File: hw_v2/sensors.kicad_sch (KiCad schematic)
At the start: 47 parts, among them U10 BMP280, U21 ADXL343, U23 MCP6004, U24 MCP6004, U6 TJA1051T-3

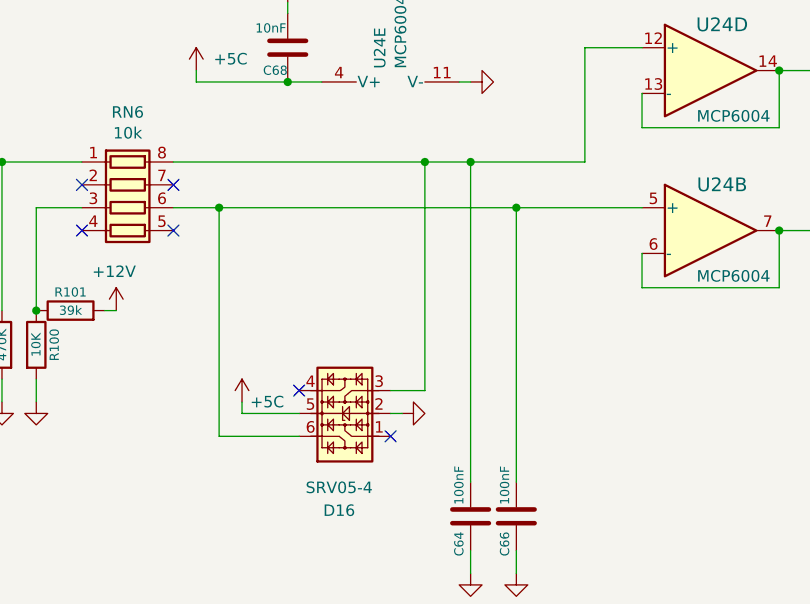
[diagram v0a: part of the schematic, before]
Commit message: wip routing iny/ign drivers
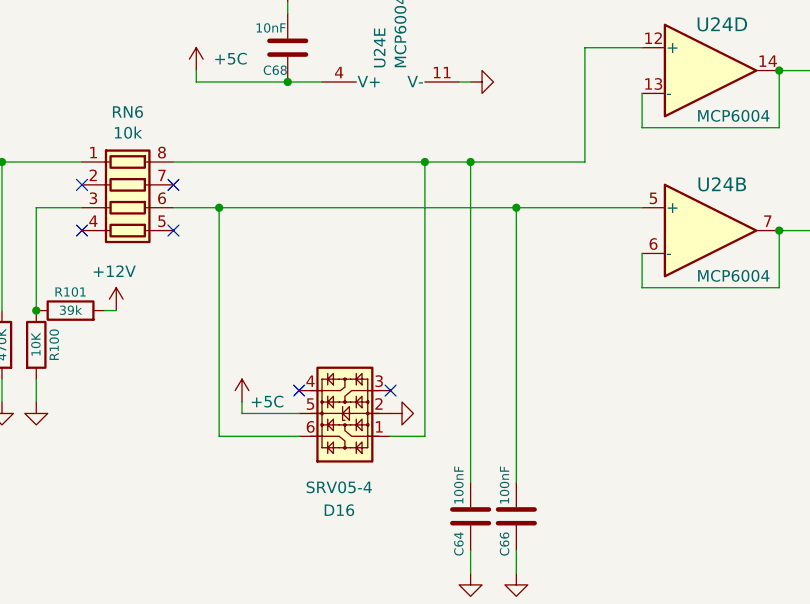
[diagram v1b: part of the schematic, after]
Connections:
- net at C64.1, RN6.8 (R1.2), U24.12 (+): now also D16.1; no longer D16.3
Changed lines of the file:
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@@
 	)
 	(no_connect
-		(at 100.33 160.02)
+		(at 100.33 154.94)
 	)
 	(no_connect
@@
 	(wire
 		(pts
-			(xy 100.33 157.48) (xy 101.6 157.48)
-		)
-		(stroke
-			(width 0)
-			(type default)
-		)
-	)
-	(wire
-		(pts
 			(xy 72.39 53.34) (xy 72.39 81.28)
 		)
@@
 	(wire
 		(pts
-			(xy 104.14 154.94) (xy 104.14 129.54)
-		)
-		(stroke
-			(width 0)
-			(type default)
-		)
-	)
-	(wire
-		(pts
 			(xy 158.75 119.38) (xy 168.91 119.38)
 		)
@@
 	(wire
 		(pts
+			(xy 104.14 129.54) (xy 104.14 160.02)
+		)
+		(stroke
+			(width 0)
+			(type default)
+		)
+	)
+	(wire
+		(pts
 			(xy 275.59 123.19) (xy 273.05 123.19)
 		)
@@
 	(wire
 		(pts
-			(xy 104.14 154.94) (xy 100.33 154.94)
+			(xy 143.51 137.16) (xy 147.32 137.16)
 		)
 		(stroke
@@
 	(wire
 		(pts
-			(xy 143.51 137.16) (xy 147.32 137.16)
+			(xy 68.58 48.26) (xy 88.9 48.26)
 		)
 		(stroke
@@
 	(wire
 		(pts
-			(xy 68.58 48.26) (xy 88.9 48.26)
+			(xy 100.33 160.02) (xy 104.14 160.02)
 		)
 		(stroke
@@
 	(symbol
 		(lib_id "power:GND")
-		(at 101.6 157.48 90)
+		(at 100.33 157.48 90)
 		(unit 1)
 		(exclude_from_sim no)
@@
 		(dnp no)
 		(property "Reference" "#PWR0189"
-			(at 101.6 157.48 0)
+			(at 100.33 157.48 0)
 			(effects
 				(font
@@
 		)
 		(property "Value" "GND"
-			(at 103.378 157.48 0)
+			(at 102.108 157.48 0)
 			(effects
 				(font
@@
 		)
 		(property "Footprint" ""
-			(at 101.6 157.48 0)
+			(at 100.33 157.48 0)
 			(effects
 				(font
@@
 		)
 		(property "Datasheet" ""
-			(at 101.6 157.48 0)
+			(at 100.33 157.48 0)
 			(effects
 				(font
@@
 		)
 		(property "Description" "Power symbol creates a global label with name \"GND\" , ground"
-			(at 101.6 157.48 0)
+			(at 100.33 157.48 0)
 			(effects
 				(font

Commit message: update ADC oamp
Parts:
- U23, U24: value MCP6004 -> LMV324IPWR; LCSC C248577 -> (none)
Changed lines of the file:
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@@
 			)
 		)
-		(property "Value" "MCP6004"
+		(property "Value" "LMV324IPWR"
 			(at 101.473 119.1768 0)
 			(effects
@@
 			)
 		)
-		(property "LCSC" "C248577"
+		(property "LCSC" ""
 			(at 100.33 118.11 0)
 			(effects
@@
 			)
 		)
-		(property "Value" "MCP6004"
+		(property "Value" "LMV324IPWR"
 			(at 124.46 78.74 0)
 			(effects
@@
 			)
 		)
-		(property "LCSC" "C248577"
+		(property "LCSC" ""
 			(at 121.92 72.39 0)
 			(effects
@@
 			)
 		)
+		(property "Campo10" ""
+			(at 121.92 72.39 0)
+			(effects
+				(font
+					(size 1.27 1.27)
+				)
+			)
+		)
 		(pin "10"
 		)
@@
 			)
 		)
-		(property "Value" "MCP6004"
+		(property "Value" "LMV324IPWR"
 			(at 149.86 194.31 0)
 			(effects
@@
 			)
 		)
-		(property "LCSC" "C248577"
+		(property "LCSC" ""
 			(at 147.32 189.23 0)
 			(effects
@@
 			)
 		)
-		(property "Value" "MCP6004"
+		(property "Value" "LMV324IPWR"
 			(at 124.46 53.34 0)
 			(effects
@@
 			)
 		)
-		(property "LCSC" "C248577"
+		(property "LCSC" ""
 			(at 121.92 46.99 0)
 			(effects
@@
 			)
 		)
+		(property "Campo10" ""
+			(at 121.92 46.99 0)
+			(effects
+				(font
+					(size 1.27 1.27)
+				)
+			)
+		)
 		(pin "5"
 		)
@@
 			)
 		)
-		(property "Value" "MCP6004"
+		(property "Value" "LMV324IPWR"
 			(at 124.46 40.64 0)
 			(effects
@@
 			)
 		)
-		(property "LCSC" "C248577"
+		(property "LCSC" ""
 			(at 121.92 34.29 0)
 			(effects
@@
 			)
 		)
+		(property "Campo10" ""
+			(at 121.92 34.29 0)
+			(effects
+				(font
+					(size 1.27 1.27)
+				)
+			)
+		)
 		(pin "1"
 		)
@@
 			)
 		)
-		(property "Value" "MCP6004"
+		(property "Value" "LMV324IPWR"
 			(at 124.46 66.04 0)
 			(effects
@@
 			)
 		)
-		(property "LCSC" "C248577"
+		(property "LCSC" ""
 			(at 121.92 59.69 0)
 			(effects
@@
 			)
 		)
+		(property "Campo10" ""
+			(at 121.92 59.69 0)
+			(effects
+				(font
+					(size 1.27 1.27)
+				)
+			)
+		)
 		(pin "12"
 		)
@@
 			)
 		)
-		(property "Value" "MCP6004"
+		(property "Value" "LMV324IPWR"
 			(at 138.43 124.46 0)
 			(effects
@@
 			)
 		)
-		(property "LCSC" "C248577"
+		(property "LCSC" ""
 			(at 135.89 119.38 0)
 			(effects
@@
 			)
 		)
-		(property "Value" "MCP6004"
+		(property "Value" "LMV324IPWR"
 			(at 167.64 194.31 0)
 			(effects
@@
 			)
 		)
-		(property "LCSC" "C248577"
+		(property "LCSC" ""
 			(at 165.1 189.23 0)
 			(effects
@@
 			)
 		)
-		(property "Value" "MCP6004"
+		(property "Value" "LMV324IPWR"
 			(at 138.43 142.24 0)
 			(effects
@@
 			)
 		)
-		(property "LCSC" "C248577"
+		(property "LCSC" ""
 			(at 135.89 137.16 0)
 			(effects
@@
 			)
 		)
-		(property "Value" "MCP6004"
+		(property "Value" "LMV324IPWR"
 			(at 44.577 67.5132 0)
 			(effects
@@
 			)
 		)
-		(property "LCSC" "C248577"
+		(property "LCSC" ""
 			(at 45.72 68.58 0)
 			(effects
@@
 			)
 		)
+		(property "Campo10" ""
+			(at 45.72 68.58 0)
+			(effects
+				(font
+					(size 1.27 1.27)
+				)
+			)
+		)
